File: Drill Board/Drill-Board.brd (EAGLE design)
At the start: 92.7 x 57.4 mm, 37 parts, among them J1 SL03THROUGH_HOLE, J2 SL03THROUGH_HOLE, J3 APP_2POS_CONFIG5V_HORIZ, J4 SL02-HORIZ, J6 SL03THROUGH_HOLE, U1 OKI-78SR-5/1.5-W36HC

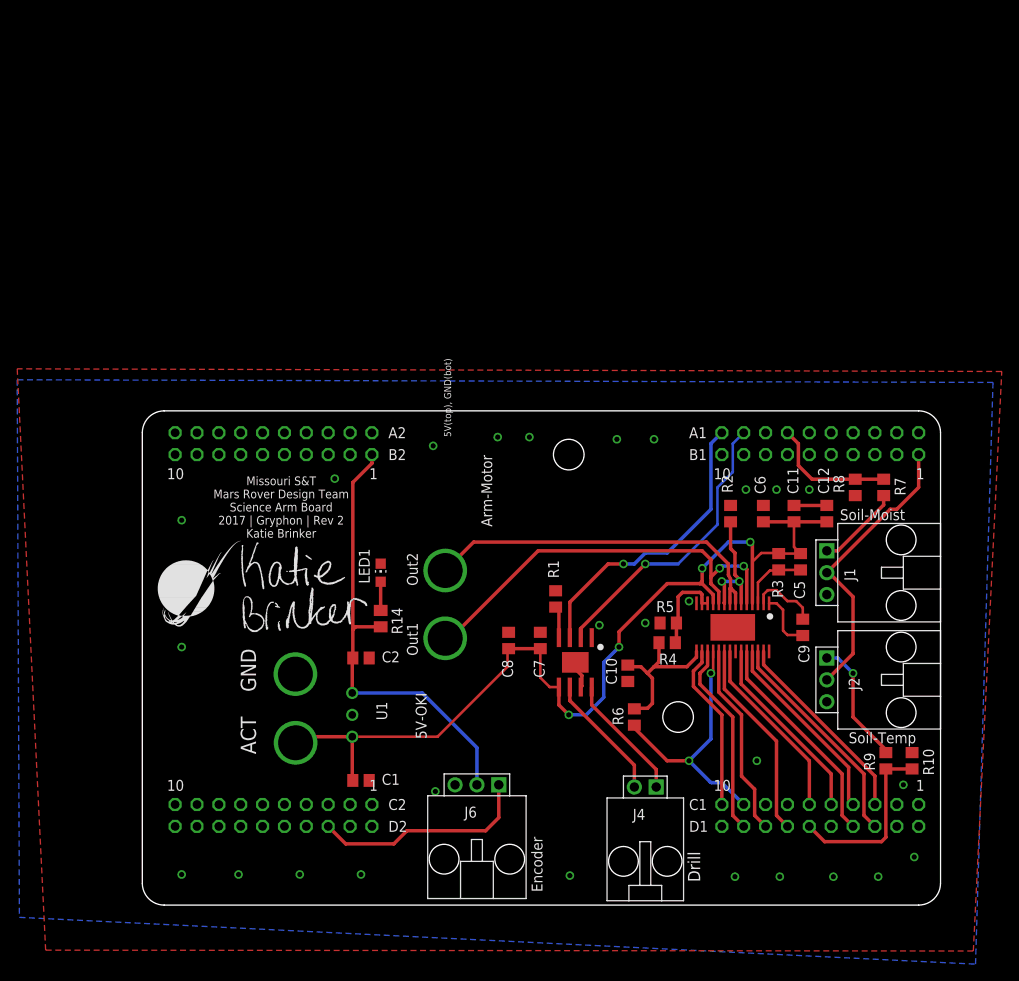
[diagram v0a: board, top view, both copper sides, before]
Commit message: Drill Board: Starting from a clean slate (power and filtering only)
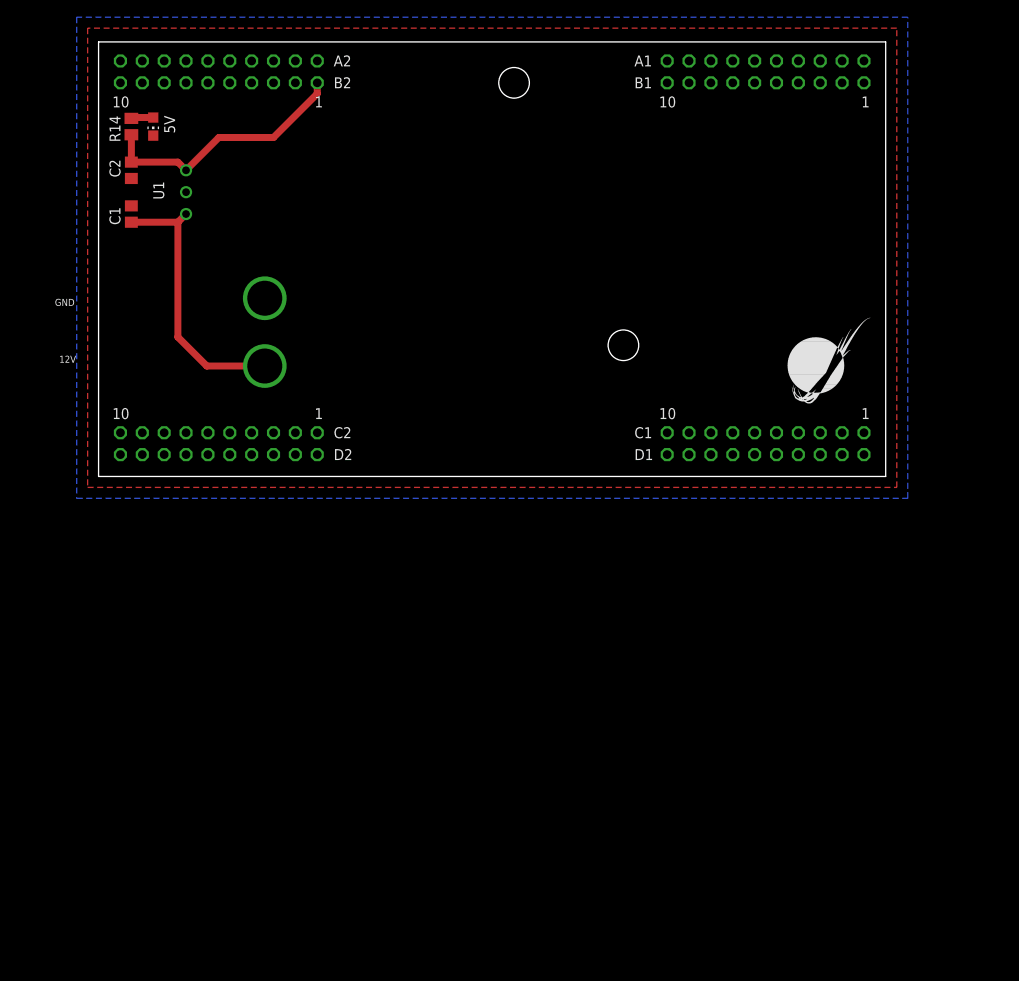
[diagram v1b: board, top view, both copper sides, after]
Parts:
- removed ACT, GND: APPPP45_PCB_HORIZ_RIGHT, MRDT-Connectors:APP45_PCB_HORIZ_RIGHT
- removed C10: 0.47uF, rcl:C0805
- removed C11: 100uF, rcl:C0805
- removed C12, C5, C6, C7: 0.1uF, rcl:C0805
- removed C8: 47uF, rcl:C0805
- removed C9: 0.01uF, rcl:C0805
- removed J2, J6: SL03THROUGH_HOLE, MRDT-Connectors:MOLEX_SL_03_TH
- removed J3: APP_2POS_CONFIG5V_HORIZ, MRDT-Connectors:APP45_5V_HORIZ_CONFIG
- removed J4: SL02-HORIZ, MRDT-Connectors:MOLEX-70551-0001
- removed LED1: (no value), led:CHIP-LED0805
- removed R1: 30k, rcl:R0805
- removed R10, R8: 19.3k, rcl:R0805
- removed R2: 100m, rcl:R0805
- removed R3: 1M, rcl:R0805
- removed R4: 34k, rcl:R0805
- removed R5, R6, R7, R9: 10k, rcl:R0805
- removed U$2: DRV8842, DRV8842:DRV8842
- removed U$3: DRV8871, drill-motor-driver:DRV8871
- removed U$5: KATIE-BRINKER, sig:KATIE-BRINKER-SIG
- added 5V: (no value), led:CHIP-LED0805
- J1: value SL03THROUGH_HOLE -> APP_2POS_CONFIG12V_HORIZ; device MRDT-Connectors:MOLEX_SL_03_TH -> MRDT-Connectors:APP45_12V_HORIZ_CONFIG
- moved J1 95.6 mm to (-8.89, 58.4), turned to 0 degrees
- moved LOGO1 77.6 mm to (80.0, 57.1)
- moved C1 71.0 mm to (3.81, 80.0), turned to 90 degrees
- moved R14 64.1 mm to (3.81, 90.2)
- moved U1 63.7 mm to (10.2, 80.0)
- moved C2 62.6 mm to (3.81, 85.1), turned to 270 degrees
- moved H1 43.6 mm to (48.3, 95.2)
- moved U$1 43.6 mm to (-34.3, 43.2)
- moved H5 43.6 mm to (61.0, 64.8)
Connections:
- removed net 3V3: C10.1, R4.2, R6.1, U$2.V3P3OUT
- removed net N$1: R1.1, U$3.ILIM
- removed net N$2: J4.1, U$3.OUT2
- removed net N$3: R2.1, U$2.ISEN, U$2.ISEN1
- removed net N$35: J1.1, R7.2
- removed net N$36: J2.1, R9.2
- removed net N$6: C9.2, U$2.CP1
- removed net N$7: C9.1, U$2.CP2
- removed net N$8: C5.1, R3.1, U$2.VCP
- removed net N$9: R4.1, R5.2, U$2.VREF, U$2.VREF1
- removed net OUT1: J4.2, U$3.OUT1
- removed net OUTPUT1: J3.5V, U$2.OUT1, U$2.OUTPUT1
- removed net OUTPUT2: J3.GND, U$2.OUT2, U$2.OUTPUT2
- net 12V-ACT: now also J1.12V; no longer ACT.P$1, C11.1, C12.1, C5.2, C6.1, C7.1, C8.1, R3.2, U$2.VM, U$2.VM1, U$3.VM
- net 5V-EXT: no longer J1.2, J2.2, J6.2
- net DECAY: no longer U$2.DECAY
- net ENCODER-OUT: no longer J6.1
- net FAULT: no longer R6.2, U$2.NFAULT
- net GND: now also 5V.C, J1.GND; no longer C10.2, C11.2, C12.2, C6.2, C7.2, C8.2, GND.P$1, J1.3, J2.3, J6.3, LED1.C, R1.2, R10.1, R2.2, R5.1, R8.1, U$2.GND, U$2.GND1, U$2.PPAD, U$3.GND, U$3.PGND, U$3.PPAD
- net I0: no longer U$2.I0
- net I1: no longer U$2.I1
- net I2: no longer U$2.I2
- net I3: no longer U$2.I3
- net I4: no longer U$2.I4
- net IN1-DRILL: no longer U$3.IN1
- net IN1-MAIN: no longer U$2.IN1
- net IN2-DRILL: no longer U$3.IN2
- net IN2-MAIN: no longer U$2.IN2
- net N$37: now also 5V.A; no longer LED1.A
- net RESET: no longer U$2.NRESET
- net SLEEP: no longer U$2.NSLEEP
- net SOIL-MOIST: no longer R7.1, R8.2
- net SOIL-TEMP: no longer R10.2, R9.1
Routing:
- net 12V-ACT: track 115.1 -> 31.6 mm, vias 4 -> 0
- net 5V-EXT: track 87.1 -> 30.1 mm
- net OUTPUT1: track 49.8 -> 0.00 mm, vias 2 -> 0
- net OUTPUT2: track 42.0 -> 0.00 mm
- net IN1-DRILL: track 34.4 -> 0.00 mm, vias 1 -> 0
- net IN2-DRILL: track 33.9 -> 0.00 mm, vias 1 -> 0
- net FAULT: track 30.8 -> 0.00 mm, vias 2 -> 0
- net I3: track 25.9 -> 0.00 mm
- net ENCODER-OUT: track 25.7 -> 0.00 mm
- net I1: track 25.4 -> 0.00 mm
- net IN2-MAIN: track 23.4 -> 0.00 mm
- net I4: track 23.1 -> 0.00 mm
- net SLEEP: track 22.8 -> 0.00 mm
- net I2: track 22.6 -> 0.00 mm
- net DECAY: track 22.6 -> 0.00 mm
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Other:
- board size 92.7 x 57.4 mm -> 91.4 x 50.5 mm
- board text removed: "5V-OKI"
- board text removed: "ACT"
- board text removed: "Arm-Motor"
- board text removed: "Drill"
- board text removed: "Encoder"
- board text removed: "GND"
- board text removed: "Missouri S&T Mars Rover Design Team Science Arm Board 2017 | Gryphon | Rev 2 Katie Brinker"
- board text removed: "Out1"
- board text removed: "Out2"
- board text removed: "Soil-Moist"
- board text removed: "Soil-Temp"
